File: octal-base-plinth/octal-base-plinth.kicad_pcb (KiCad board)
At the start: 2 copper layers, 100 x 100 mm, 14 parts

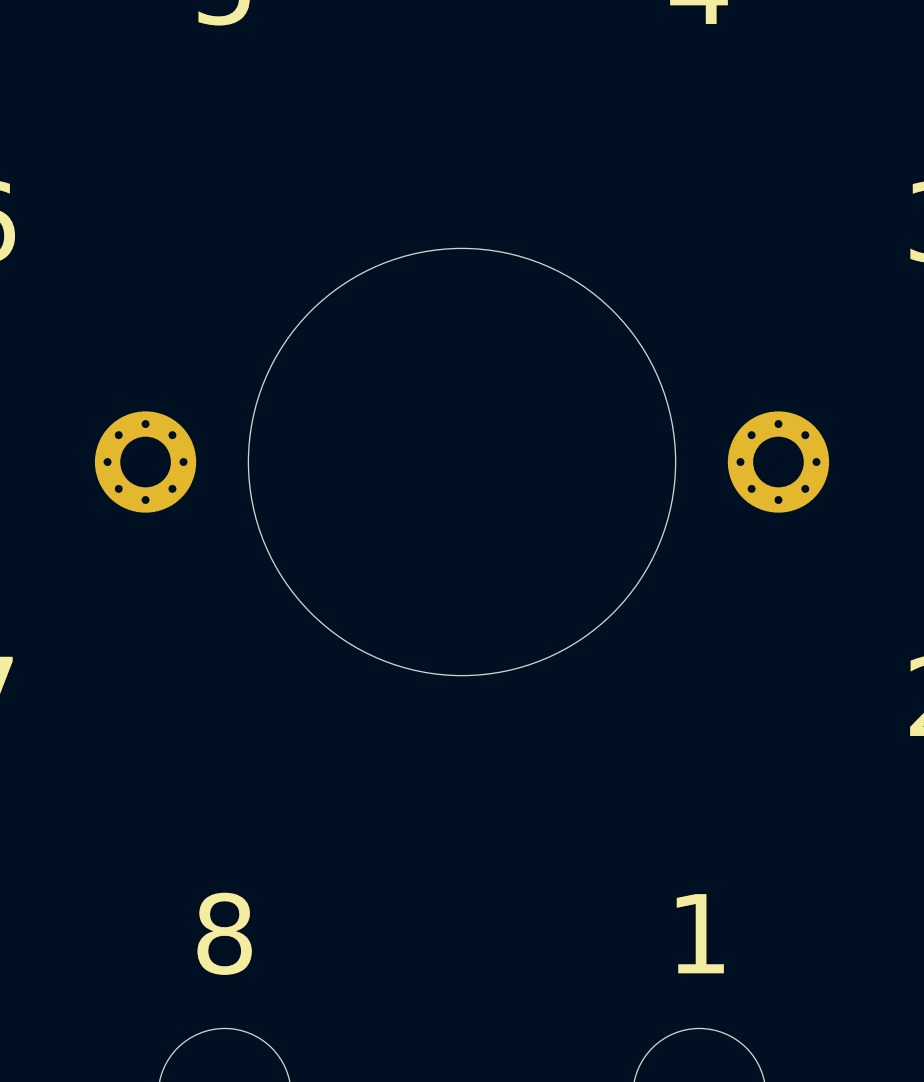
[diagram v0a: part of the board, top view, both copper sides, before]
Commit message: Moved the mounting screws to support two types of socket.
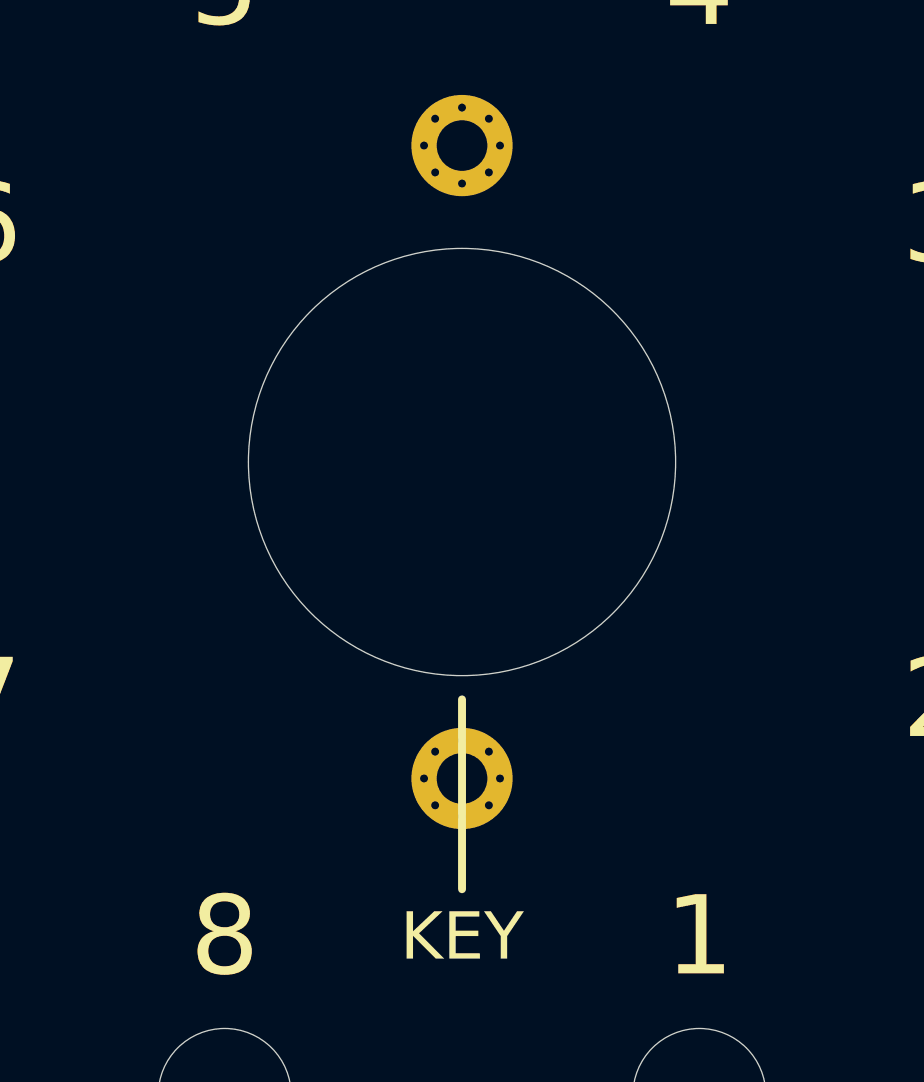
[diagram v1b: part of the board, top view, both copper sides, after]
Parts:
- moved e 28.3 mm to (100.0, 80.0)
- moved e 28.3 mm to (100.0, 120.0)
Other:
- board text added: "KEY"
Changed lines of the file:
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@@
   (general
     (thickness 1.6)
-    (drawings 26)
+    (drawings 28)
     (tracks 0)
     (zones 0)
@@
   )
   (module MountingHole:MountingHole_3.2mm_M3_Pad_Via (layer F.Cu)
-    (at 80 100)
-    (descr "Mounting Hole 3.2mm, M3")
-    (tags "mounting hole 3.2mm m3")
-    (attr virtual)
-    (fp_text reference e (at 0 -4.2) (layer F.SilkS) hide
-      (effects (font (size 1 1) (thickness 0.15)))
-    )
-    (fp_text value MountingHole_3.2mm_M3_Pad_Via (at 0 4.2) (layer F.Fab) hide
-      (effects (font (size 1 1) (thickness 0.15)))
-    )
-    (fp_text user %R (at 0.3 0) (layer F.Fab) hide
-      (effects (font (size 1 1) (thickness 0.15)))
-    )
-    (fp_circle (center 0 0) (end 3.2 0) (layer Cmts.User) (width 0.15))
-    (fp_circle (center 0 0) (end 3.45 0) (layer F.CrtYd) (width 0.05))
-    (pad 1 thru_hole circle (at 0 0) (size 6.4 6.4) (drill 3.2) (layers *.Cu *.Mask))
-    (pad 1 thru_hole circle (at 2.4 0) (size 0.8 0.8) (drill 0.5) (layers *.Cu *.Mask))
-    (pad 1 thru_hole circle (at 1.697056 1.697056) (size 0.8 0.8) (drill 0.5) (layers *.Cu *.Mask))
-    (pad 1 thru_hole circle (at 0 2.4) (size 0.8 0.8) (drill 0.5) (layers *.Cu *.Mask))
-    (pad 1 thru_hole circle (at -1.697056 1.697056) (size 0.8 0.8) (drill 0.5) (layers *.Cu *.Mask))
-    (pad 1 thru_hole circle (at -2.4 0) (size 0.8 0.8) (drill 0.5) (layers *.Cu *.Mask))
-    (pad 1 thru_hole circle (at -1.697056 -1.697056) (size 0.8 0.8) (drill 0.5) (layers *.Cu *.Mask))
-    (pad 1 thru_hole circle (at 0 -2.4) (size 0.8 0.8) (drill 0.5) (layers *.Cu *.Mask))
-    (pad 1 thru_hole circle (at 1.697056 -1.697056) (size 0.8 0.8) (drill 0.5) (layers *.Cu *.Mask))
-  )
-  (module MountingHole:MountingHole_3.2mm_M3_Pad_Via (layer F.Cu)
-    (at 120 100)
+    (at 100 80)
+    (descr "Mounting Hole 3.2mm, M3")
+    (tags "mounting hole 3.2mm m3")
+    (attr virtual)
+    (fp_text reference e (at 0 -4.2) (layer F.SilkS) hide
+      (effects (font (size 1 1) (thickness 0.15)))
+    )
+    (fp_text value MountingHole_3.2mm_M3_Pad_Via (at 0 4.2) (layer F.Fab) hide
+      (effects (font (size 1 1) (thickness 0.15)))
+    )
+    (fp_text user %R (at 0.3 0) (layer F.Fab) hide
+      (effects (font (size 1 1) (thickness 0.15)))
+    )
+    (fp_circle (center 0 0) (end 3.2 0) (layer Cmts.User) (width 0.15))
+    (fp_circle (center 0 0) (end 3.45 0) (layer F.CrtYd) (width 0.05))
+    (pad 1 thru_hole circle (at 0 0) (size 6.4 6.4) (drill 3.2) (layers *.Cu *.Mask))
+    (pad 1 thru_hole circle (at 2.4 0) (size 0.8 0.8) (drill 0.5) (layers *.Cu *.Mask))
+    (pad 1 thru_hole circle (at 1.697056 1.697056) (size 0.8 0.8) (drill 0.5) (layers *.Cu *.Mask))
+    (pad 1 thru_hole circle (at 0 2.4) (size 0.8 0.8) (drill 0.5) (layers *.Cu *.Mask))
+    (pad 1 thru_hole circle (at -1.697056 1.697056) (size 0.8 0.8) (drill 0.5) (layers *.Cu *.Mask))
+    (pad 1 thru_hole circle (at -2.4 0) (size 0.8 0.8) (drill 0.5) (layers *.Cu *.Mask))
+    (pad 1 thru_hole circle (at -1.697056 -1.697056) (size 0.8 0.8) (drill 0.5) (layers *.Cu *.Mask))
+    (pad 1 thru_hole circle (at 0 -2.4) (size 0.8 0.8) (drill 0.5) (layers *.Cu *.Mask))
+    (pad 1 thru_hole circle (at 1.697056 -1.697056) (size 0.8 0.8) (drill 0.5) (layers *.Cu *.Mask))
+  )
+  (module MountingHole:MountingHole_3.2mm_M3_Pad_Via (layer F.Cu)
+    (at 100 120)
     (descr "Mounting Hole 3.2mm, M3")
     (tags "mounting hole 3.2mm m3")
@@
     (pad 1 thru_hole circle (at 0 0) (size 6.4 6.4) (drill 3.2) (layers *.Cu *.Mask))
   )
+  (gr_text KEY (at 100 130) (layer F.SilkS)
+    (effects (font (size 3 3) (thickness 0.3)))
+  )
+  (gr_line (start 100 115) (end 100 127) (layer F.SilkS) (width 0.5))
   (gr_text 8 (at 85 130) (layer F.SilkS)
     (effects (font (size 5 5) (thickness 0.5)))

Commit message: Updating to KiCad 9.0
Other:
- net class Default removed
